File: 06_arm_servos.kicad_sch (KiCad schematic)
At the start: 33 parts, among them J11 SERVO 6 V TEST/OUT, J12 MAIN SWING 25 kg, J13 ELBOW MG996R, J14 WRIST MG90S, U10 TPS54560BDDA, U5 PCA9685PW

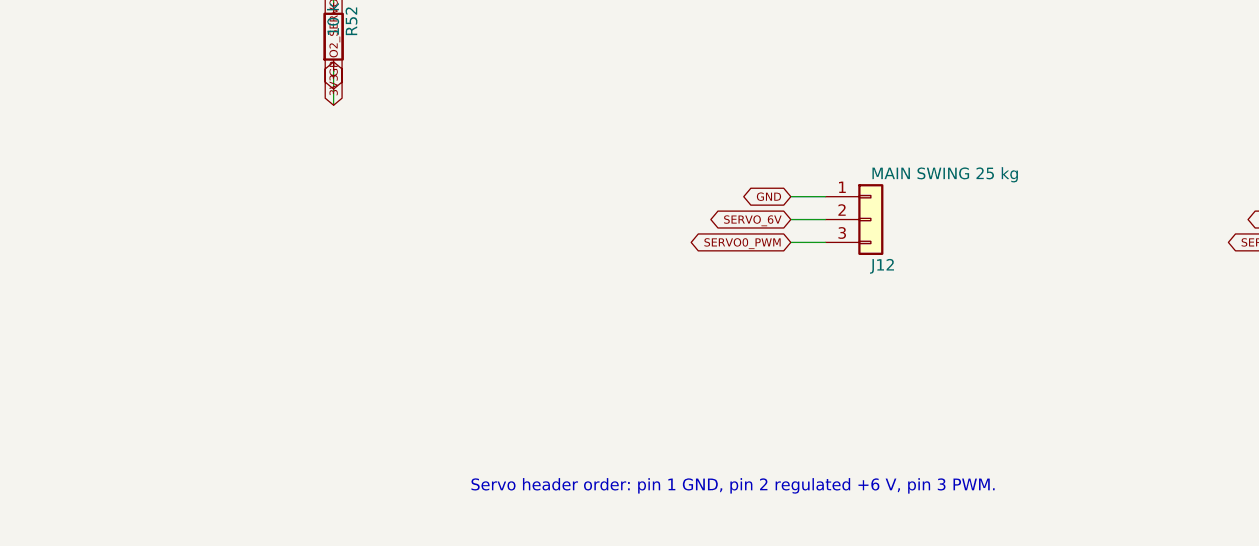
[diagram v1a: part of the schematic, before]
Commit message: Add dedicated 8.4V rail for Miuzei main servo
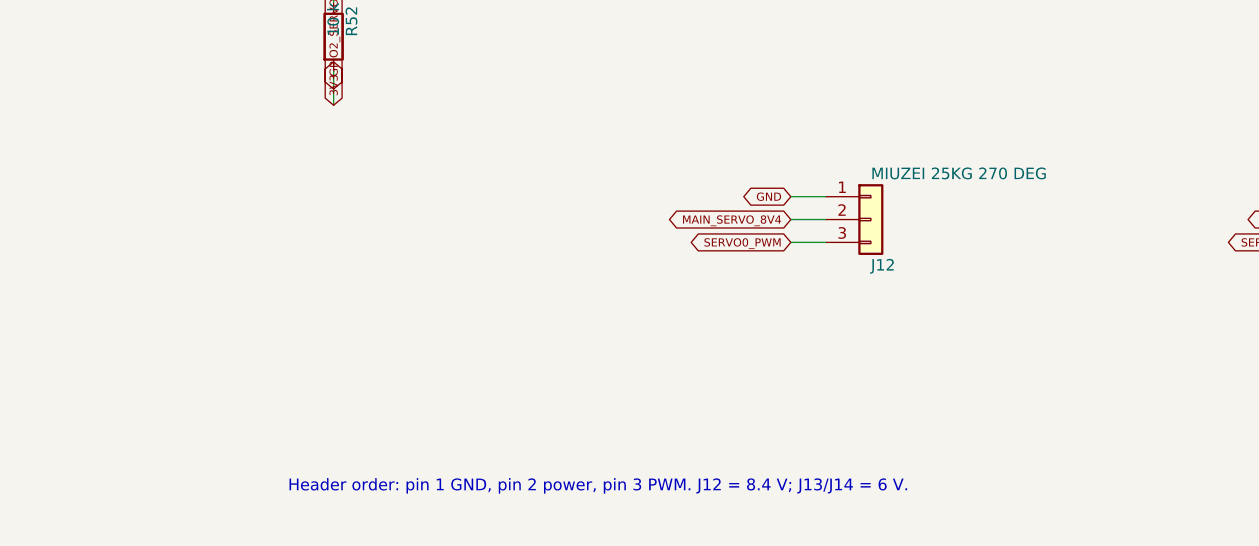
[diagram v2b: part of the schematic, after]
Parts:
- J12: value MAIN SWING 25 kg -> MIUZEI 25KG 270 DEG
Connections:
- net SERVO_6V: no longer J12.2 (Pin_2)
- new net MAIN_SERVO_8V4: J12.2 (Pin_2)
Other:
- note added: "Header order: pin 1 GND, pin 2 power, pin 3 PWM. J12 = 8.4 V; J13/J14 = 6 V."
- note removed: "Servo header order: pin 1 GND, pin 2 regulated +6 V, pin 3 PWM."

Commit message: Complete pre-PCB electrical and safety audit
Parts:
- removed C50: 220 uF 10 V, Capacitor_THT:CP_Radial_D8.0mm_P3.50mm, symbol Device:C_Polarized
- added C50, C62: 47 uF 10 V X7R, Capacitor_SMD:C_1210_3225Metric, symbol Device:C
- added C64, C65: 2.2 uF 25 V, Capacitor_SMD:C_0805_2012Metric, symbol Device:C
- added TP50: ACT_VBAT, TestPoint:TestPoint_Loop_D2.50mm_Drill1.0mm, symbol Connector:TestPoint
- added TP51: ACTUATOR_ENABLE, TestPoint:TestPoint_Loop_D2.50mm_Drill1.0mm, symbol Connector:TestPoint
- added TP52: SERVO_6V, TestPoint:TestPoint_Loop_D2.50mm_Drill1.0mm, symbol Connector:TestPoint
- added TP53: GPIO21_I2C_SDA, TestPoint:TestPoint_Loop_D2.50mm_Drill1.0mm, symbol Connector:TestPoint
- added TP54: GPIO22_I2C_SCL, TestPoint:TestPoint_Loop_D2.50mm_Drill1.0mm, symbol Connector:TestPoint
- added TP55: GPIO32_SERVO_OE, TestPoint:TestPoint_Loop_D2.50mm_Drill1.0mm, symbol Connector:TestPoint
- added TP56: GND, TestPoint:TestPoint_Loop_D2.50mm_Drill1.0mm, symbol Connector:TestPoint
- C40: value 2200 uF 10 V -> 470 uF 10 V LOW ESR; footprint Capacitor_THT:CP_Radial_D12.5mm_P5.00mm -> Capacitor_THT:CP_Radial_D10.0mm_P5.00mm
- C48: value 4.7 nF -> 5.6 nF
- C51: value 1 uF 10 V -> 47 uF 10 V X7R; footprint Capacitor_SMD:C_0805_2012Metric -> Capacitor_SMD:C_1210_3225Metric
- F2: value 7.5 A servo fuse -> 5 A MINI BLADE SERVO; footprint Fuse:Fuse_1206_3216Metric -> Fuse:Fuseholder_Blade_Mini_Keystone_3568
- R105: value 590 k -> 66.3 k 1%
- R106: value 90.9 k -> 10.2 k 1%
- R107: value 10.2 k -> 18.2 k 1%
- R52: value 10 k -> 10 k DEFAULT DISABLED
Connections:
- net GND: now also C50.2, C62.2, C64.2, C65.2, TP56.1
- net GPIO21_I2C_SDA: now also TP53.1
- net GPIO22_I2C_SCL: now also TP54.1
- net SERVO_6V: now also TP52.1
- net SERVO_6V_RAW: now also C50.1, C62.1
- net GPIO2_SERVO_OE renamed GPIO32_SERVO_OE
- net GPIO32_SERVO_OE: now also TP55.1
- net VBAT_SW renamed ACT_VBAT
- net ACT_VBAT: now also C64.1, C65.1, TP50.1; no longer U10.3 (EN)
- new net ACTUATOR_ENABLE: TP51.1, U10.3 (EN)

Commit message: Correct critical controller schematic safety issues
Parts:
- added C67: 22 uF 35 V X7R, Capacitor_SMD:C_1210_3225Metric, symbol Device:C
- added C69: DNP SNUBBER 1 nF, Capacitor_SMD:C_0805_2012Metric, symbol Device:C
- added R113: DNP SNUBBER 10 R, Resistor_SMD:R_0805_2012Metric, symbol Device:R
- C40: value 470 uF 10 V LOW ESR -> DNP OPTIONAL Panasonic EEU-FR1E471 470 uF 25 V; now not fitted
- C46, C47, C64, C65: value 2.2 uF 25 V -> 2.2 uF 25 V X7R
- C48: value 5.6 nF -> 4.7 nF
- C49: value 47 pF -> 56 pF
- C50, C51, C62: value 47 uF 10 V X7R -> 22 uF 35 V X7R
- D4: value SMBJ8.0A -> SMBJ8.0CA BIDIRECTIONAL
- R107: value 18.2 k 1% -> 15.0 k 1%
- TP50, TP52, TP53, TP54, TP55, TP56: footprint TestPoint:TestPoint_Loop_D2.50mm_Drill1.0mm -> TestPoint:TestPoint_Pad_D1.5mm; now left out of the parts list
- TP51: value ACTUATOR_ENABLE -> SERVO_POWER_ENABLE; footprint TestPoint:TestPoint_Loop_D2.50mm_Drill1.0mm -> TestPoint:TestPoint_Pad_D1.5mm; now left out of the parts list
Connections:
- net GND: now also D10.2 (A), D4.2 (A2), C67.2, C69.2; no longer D10.1 (K), D4.1 (A1)
- net SERVO_6V: now also D4.1 (A1); no longer D4.2 (A2)
- net SERVO_6V_RAW: now also C67.1
- net SERVO_BUCK_SW: now also D10.1 (K), R113.1; no longer D10.2 (A)
- net ACTUATOR_ENABLE renamed SERVO_POWER_ENABLE
- new net SERVO_SNUB: C69.1, R113.2

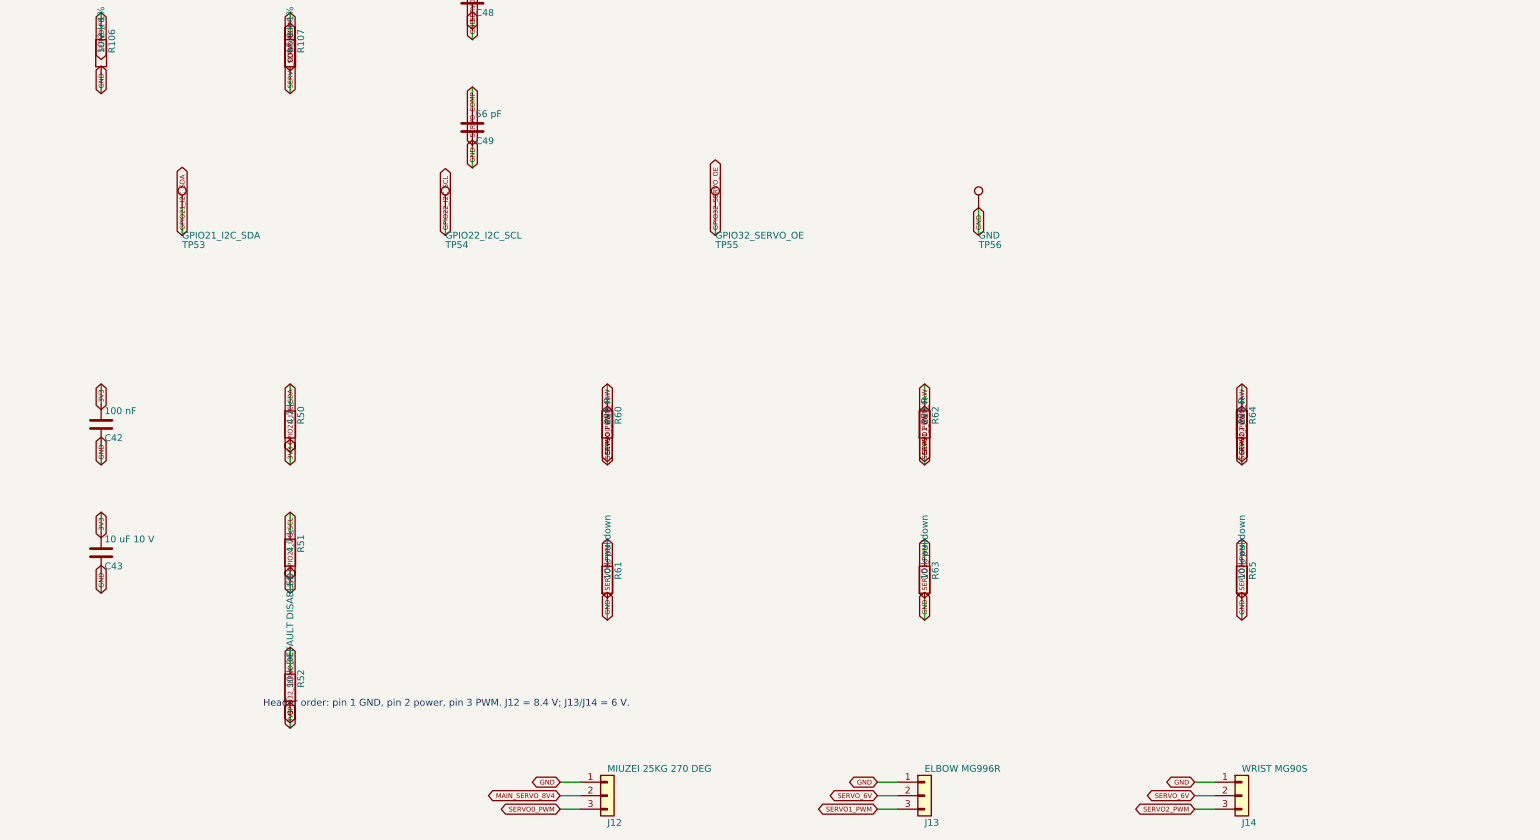
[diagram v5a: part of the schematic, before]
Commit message: Add whole-system battery cutoff and hardened servo interfaces
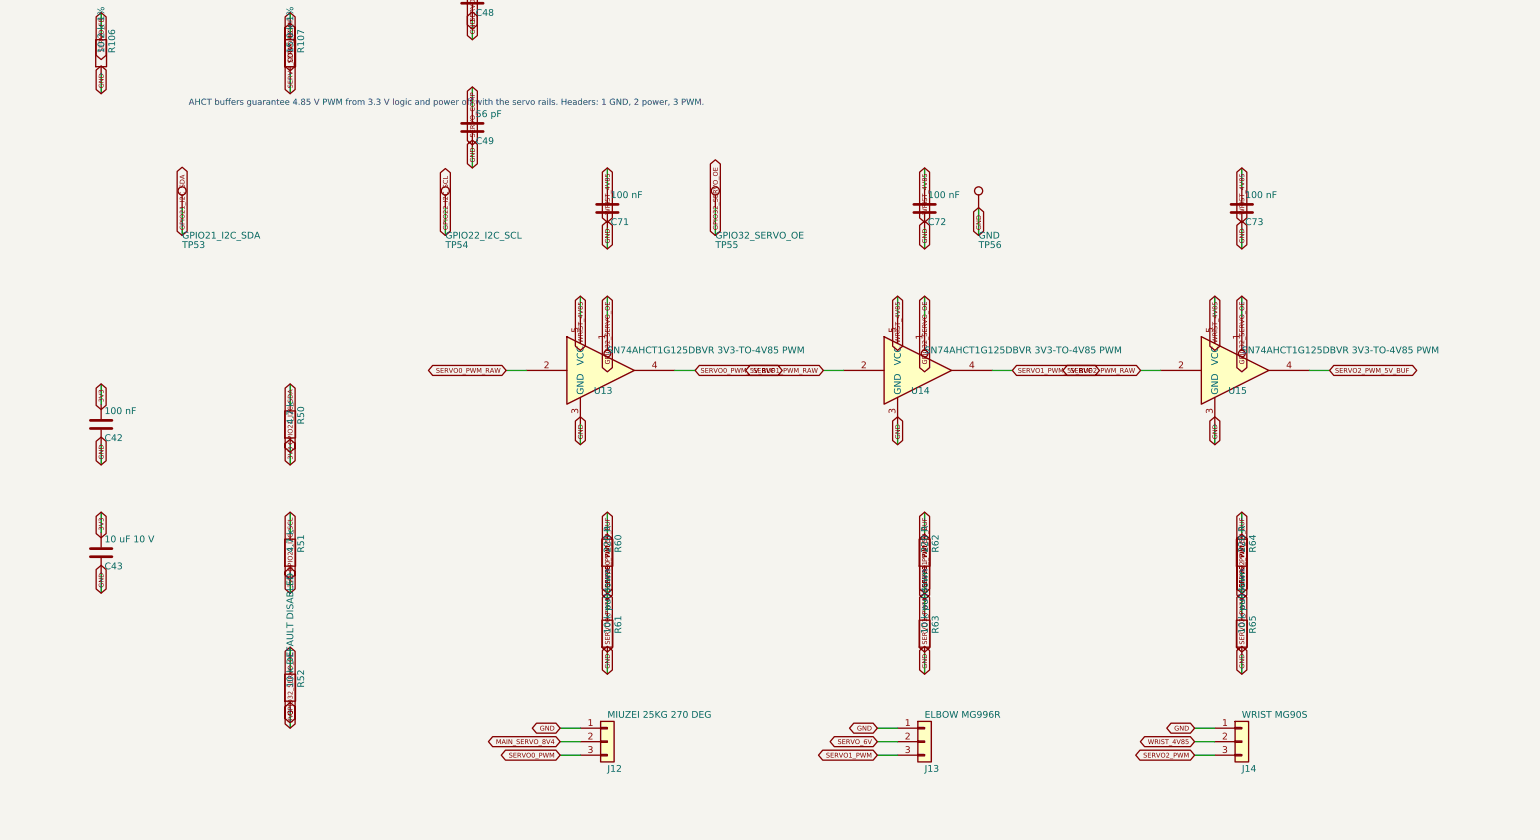
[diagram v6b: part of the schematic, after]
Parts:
- added C71, C72, C73: 100 nF, Capacitor_SMD:C_0805_2012Metric, symbol Device:C
- added U13, U14, U15: SN74AHCT1G125DBVR 3V3-TO-4V85 PWM, Package_TO_SOT_SMD:SOT-23-5_HandSoldering, symbol 74xGxx:74AHCT1G125
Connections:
- net GND: now also C71.2, C72.2, C73.2, U13.3 (GND), U14.3 (GND), U15.3 (GND)
- net GPIO32_SERVO_OE: now also U13.1, U14.1, U15.1
- net SERVO0_PWM_RAW: now also U13.2; no longer R60.1
- net SERVO1_PWM_RAW: now also U14.2; no longer R62.1
- net SERVO2_PWM_RAW: now also U15.2; no longer R64.1
- net SERVO_6V: no longer J14.2 (Pin_2)
- new net SERVO0_PWM_5V_BUF: R60.1, U13.4
- new net SERVO1_PWM_5V_BUF: R62.1, U14.4
- new net SERVO2_PWM_5V_BUF: R64.1, U15.4
- new net WRIST_4V85: C71.1, C72.1, C73.1, J14.2 (Pin_2), U13.5 (VCC), U14.5 (VCC), U15.5 (VCC)
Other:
- note added: "AHCT buffers guarantee 4.85 V PWM from 3.3 V logic and power off with the servo rails. Headers: 1 GND, 2 power, 3 PWM."
- note removed: "Header order: pin 1 GND, pin 2 power, pin 3 PWM. J12 = 8.4 V; J13/J14 = 6 V."
